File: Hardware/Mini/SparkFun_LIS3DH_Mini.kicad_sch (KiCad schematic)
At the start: 22 parts, among them J1 Conn_01x02, J2 Qwiic_RA, U1 LIS3DH

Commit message: Gets the correct shape of the Micro
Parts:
- removed J1: Conn_01x02, SparkFun-Connector:1x02, symbol SparkFun-Connector:Conn_01x02
- added J3, J4: Conn_01x01, SparkFun-Connector:1x01, symbol SparkFun-Connector:Conn_01x01
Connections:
- net GND: now also J3.1 (Pin_1)
- net INT1: now also J4.1 (Pin_1)

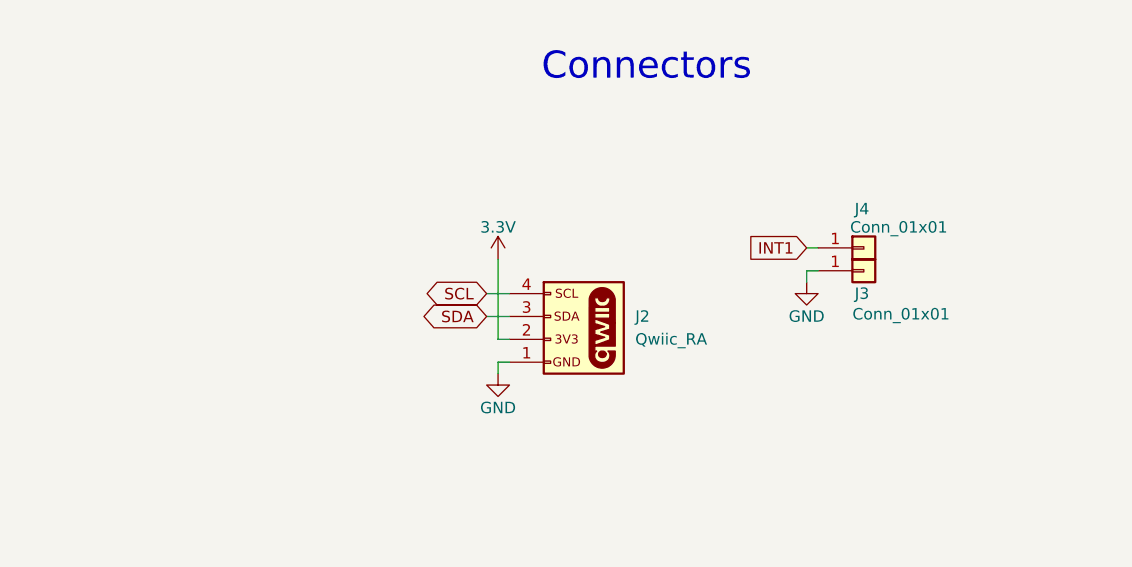
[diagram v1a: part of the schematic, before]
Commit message: Adds testpoints
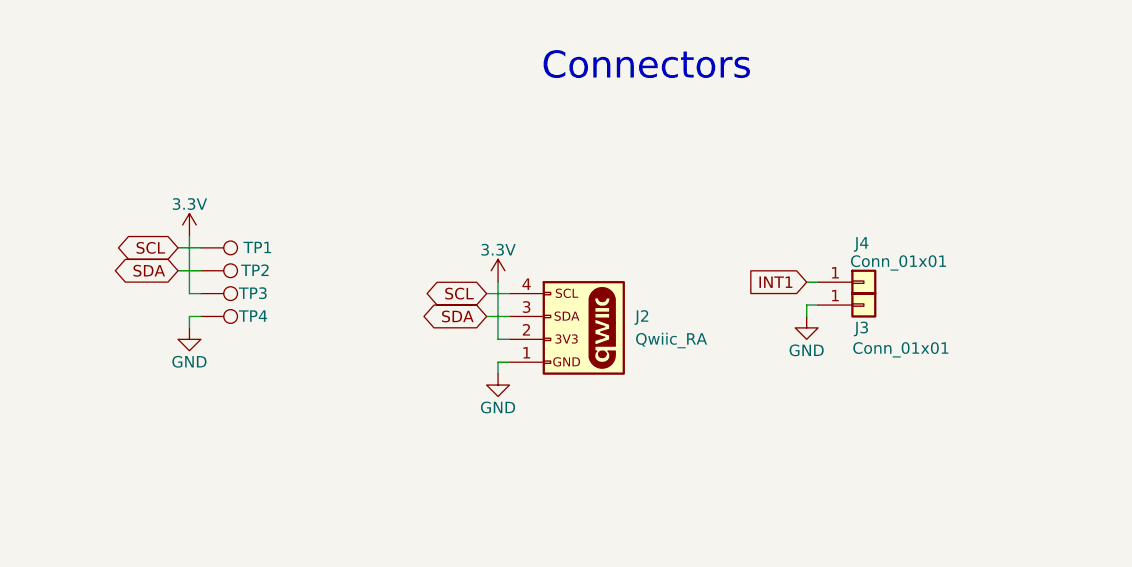
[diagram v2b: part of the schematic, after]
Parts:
- added TP1, TP2, TP3, TP4: 1.0mm, SparkFun-Connector:TestPoint-1.0mm, symbol SparkFun-Connector:TestPoint_1.0mm
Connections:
- net 3.3V: now also TP3.1
- net GND: now also TP4.1
- net SCL: now also TP1.1
- net SDA: now also TP2.1
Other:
- moved on the sheet: J3, J4

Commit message: Adds 0402 Red LED - reroutes the PCB
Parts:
- removed D1: Red, SparkFun-LED:LED_0603_1608Metric_Red, symbol SparkFun-LED:LED_Red_0603
- added D1: Red, SparkFun-LED:LED_0402_1005Metric, symbol SparkFun-LED:LED_Red_0402
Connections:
- net GND: now also D1.1 (K)
- net at R3.2: now also D1.2 (A)

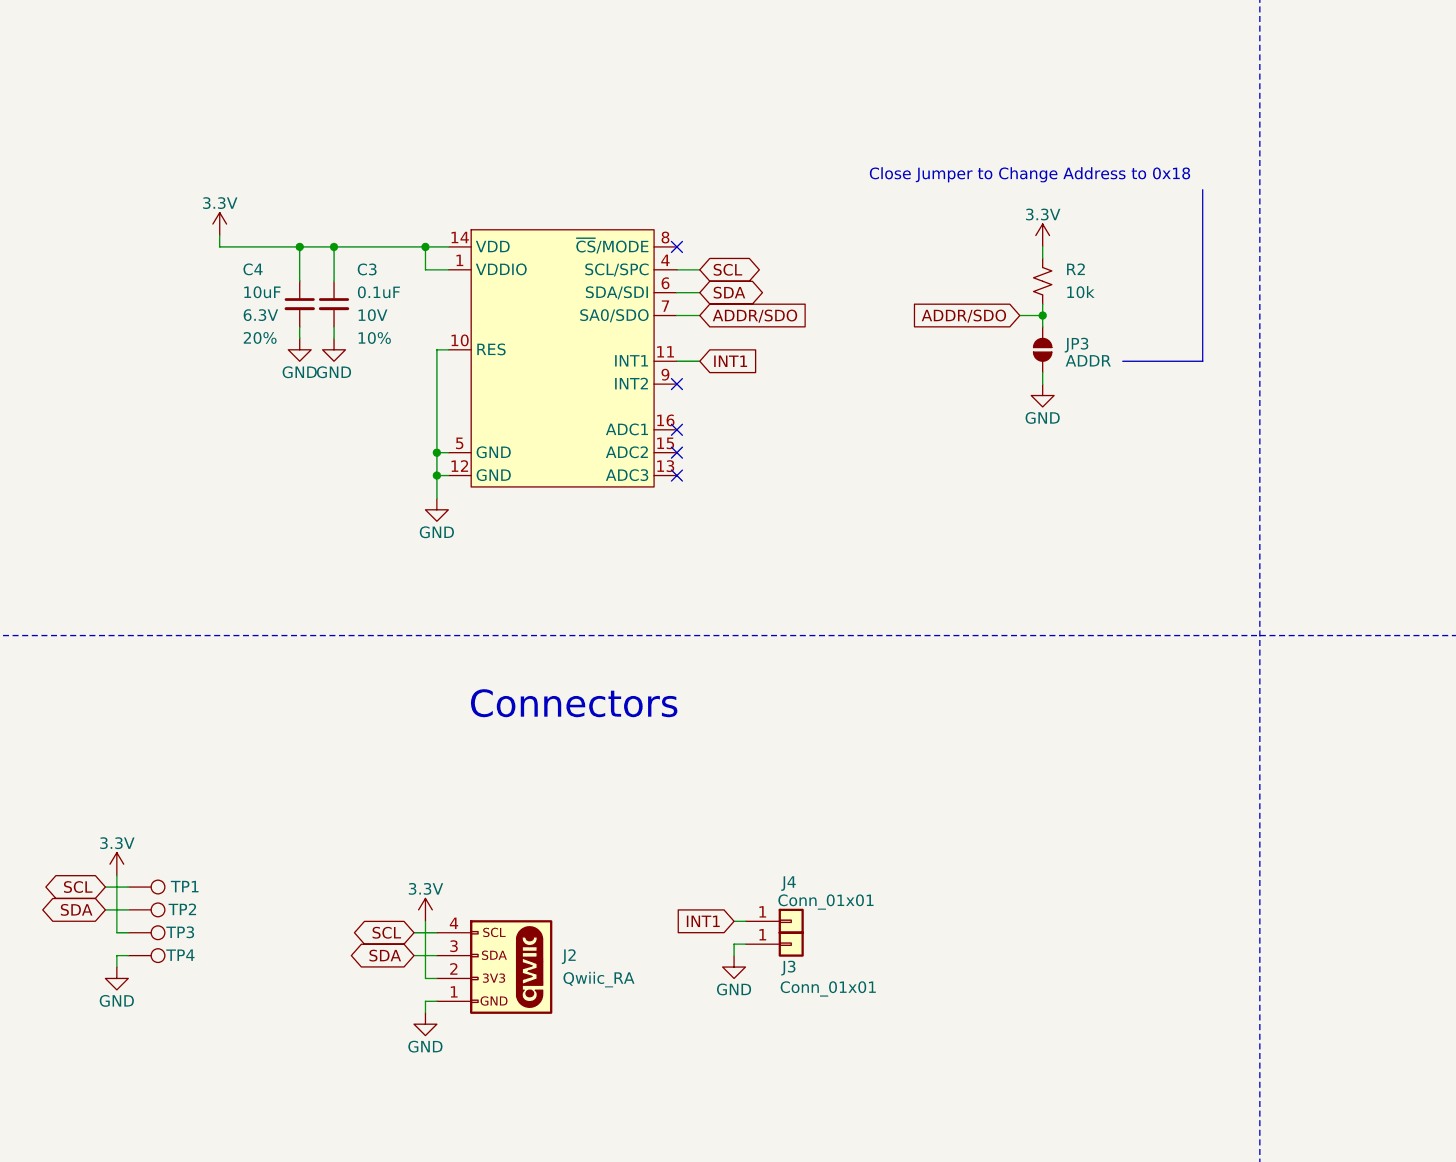
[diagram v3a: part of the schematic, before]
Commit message: Positions the testpoints according to their position in every other micro design
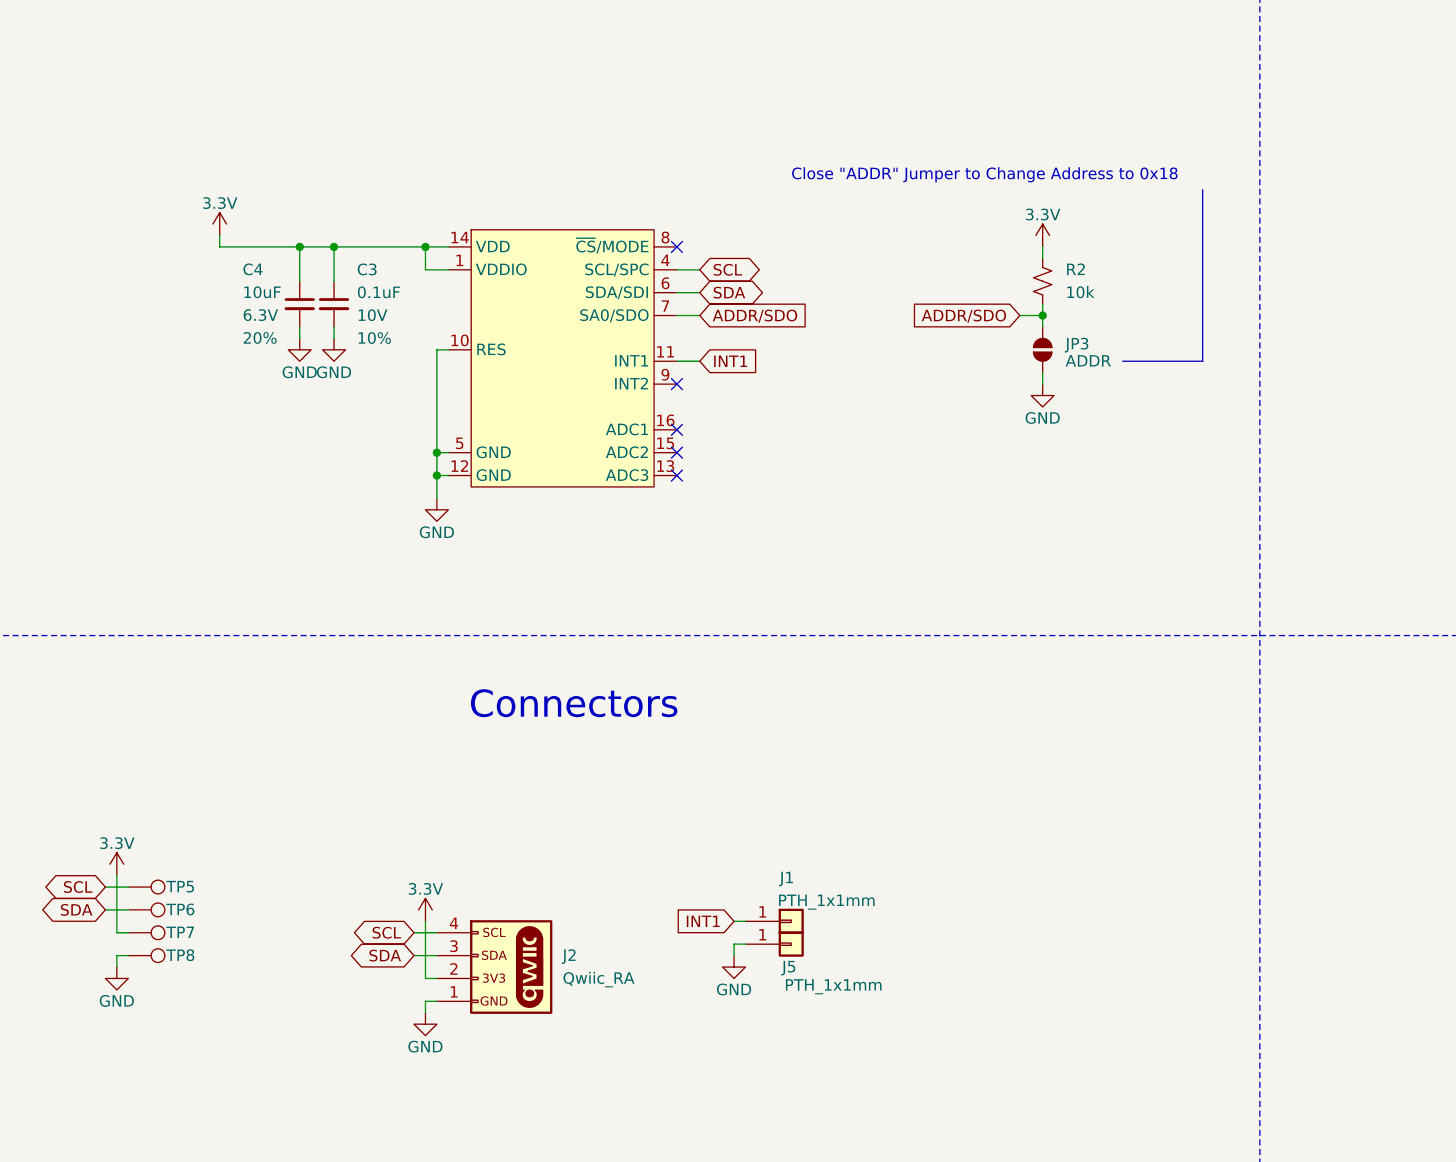
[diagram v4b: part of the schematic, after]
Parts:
- removed J3, J4: Conn_01x01, SparkFun-Connector:1x01, symbol SparkFun-Connector:Conn_01x01
- removed TP1, TP2, TP3, TP4: 1.0mm, SparkFun-Connector:TestPoint-1.0mm, symbol SparkFun-Connector:TestPoint_1.0mm
- added J1, J5: PTH_1x1mm, SparkFun-Connector:1x01_PTH_1x1mm, symbol SparkFun-Connector:Conn_01x01_PTH_1x1mm
- added TP5, TP6, TP7, TP8: 0.75mm, SparkFun-Connector:TestPoint-0.75mm, symbol SparkFun-Connector:TestPoint_0.75mm
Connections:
- net 3.3V: now also TP7.1
- net GND: now also J5.1 (Pin_1), TP8.1
- net INT1: now also J1.1 (Pin_1)
- net SCL: now also TP5.1
- net SDA: now also TP6.1
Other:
- note added: "Close "ADDR" Jumper to Change Address to 0x18"
- note removed: "Close Jumper to Change Address to 0x18"

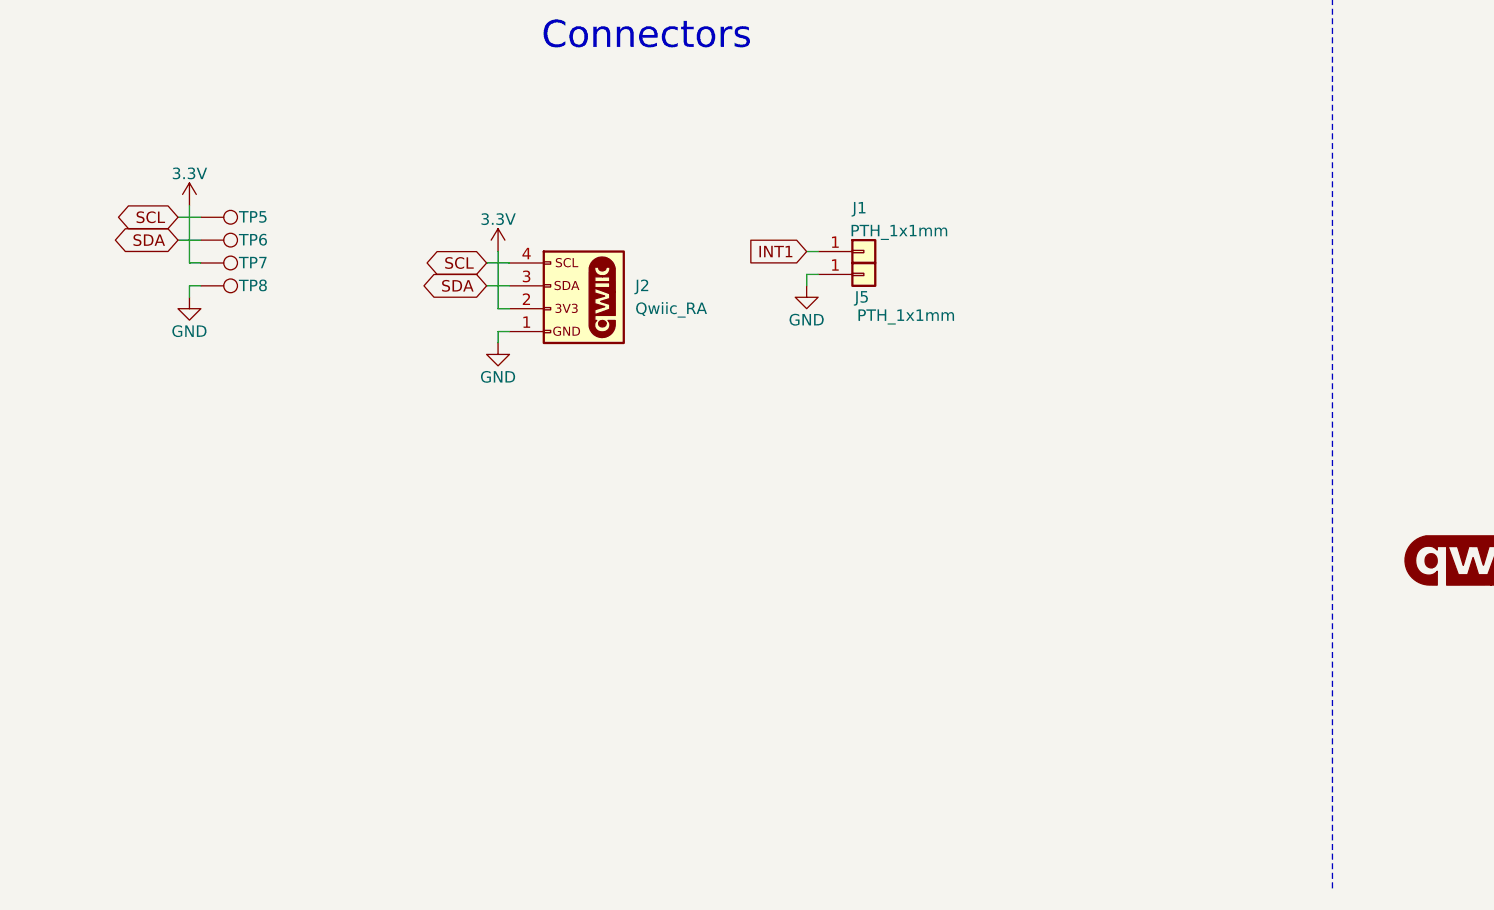
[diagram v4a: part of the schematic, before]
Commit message: Fixes measures, adjusts some traces
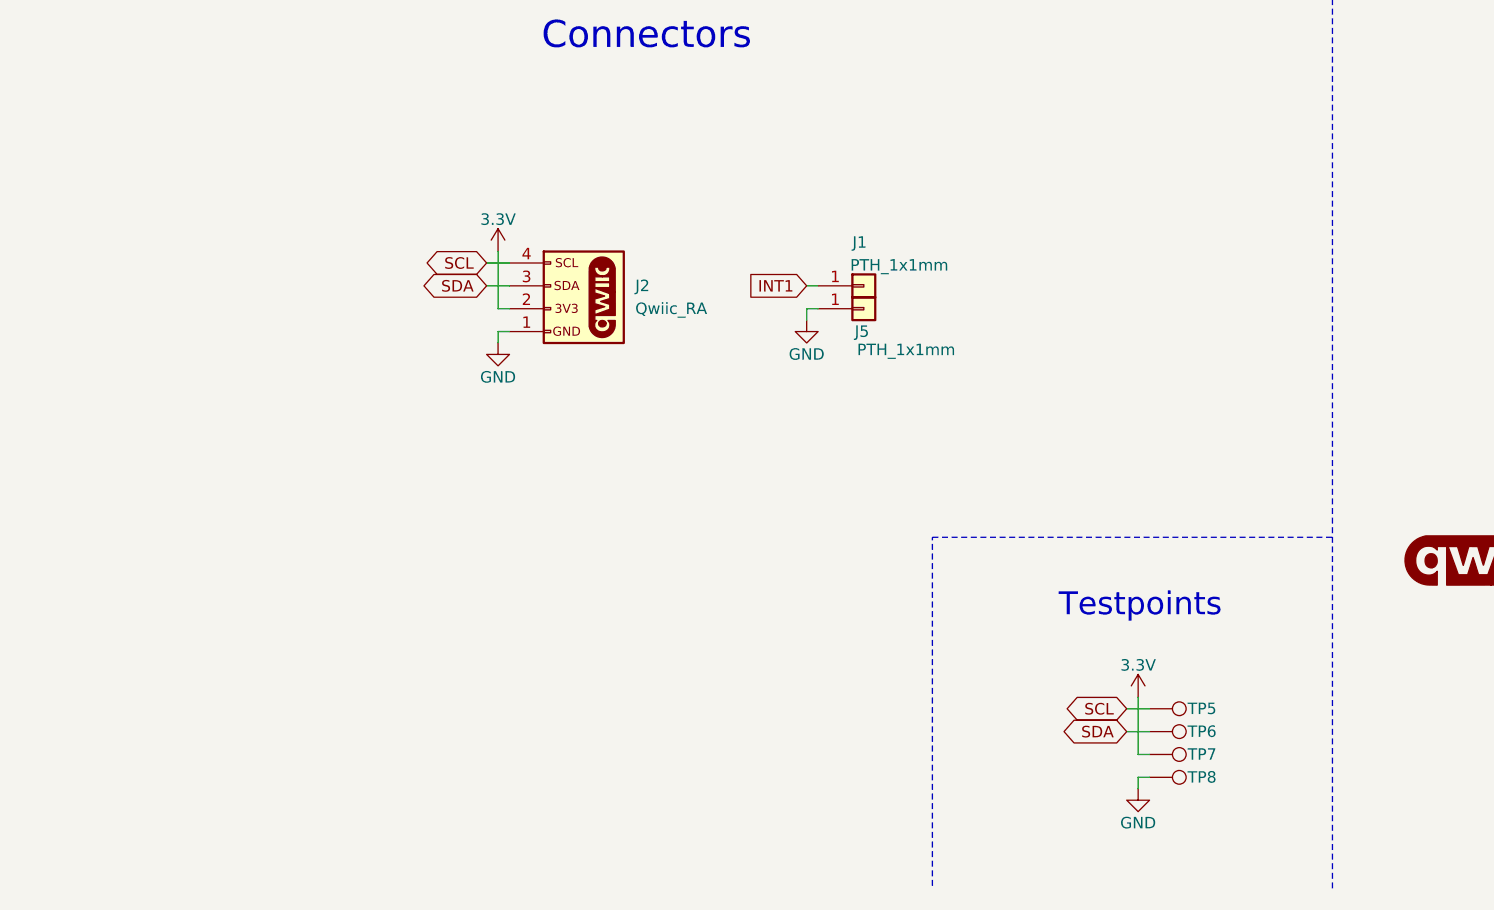
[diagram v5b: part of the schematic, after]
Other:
- note added: "Testpoints"
- moved on the sheet: J1, J5, TP5, TP6, TP7, TP8
